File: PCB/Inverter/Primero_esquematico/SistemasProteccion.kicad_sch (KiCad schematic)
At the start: 34 parts, among them U22 TLV1704AQPWRQ1, U23 TLV1704AQPWRQ1

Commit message: Esquematico practicamente terminado
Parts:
- C77, C78, C79, C80: footprint (none) -> Capacitor_SMD:C_0603_1608Metric
- R143, R144, R145, R146, R147, R148, R149, R150, R151, R152, R153, R154, R155, R156, R157, R158, R159, R160, R161, R162, R163, R164, R165, R166, R167, R168, R169, R170: footprint (none) -> Resistor_SMD:R_0402_1005Metric
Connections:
- net +3.3V_ref renamed +3V0
- removed net ErrorFlag: R144.2, R145.2, R155.2, R156.2, R162.2, R163.2, R164.2, R165.2, U22.1 (2OUT), U22.13 (4OUT), U22.14 (3OUT), U22.2 (1OUT), U23.1 (2OUT), U23.13 (4OUT), U23.14 (3OUT), U23.2 (1OUT)
- new net Error_Current_Fase_A: R144.2, R145.2, U22.1 (2OUT), U22.2 (1OUT)
- new net Error_Current_Fase_B: R155.2, R156.2, U22.13 (4OUT), U22.14 (3OUT)
- new net Error_Current_Fase_C: R162.2, R163.2, U23.1 (2OUT), U23.2 (1OUT)
- new net Error_DC: R164.2, R165.2, U23.13 (4OUT), U23.14 (3OUT)
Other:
- note added: "CALCULAR LOS LIMITE"
- note added: "Transferencia de tension medida y lo que ve el sensor en este bloque: V_sensor=V_dc.11,52mV/V-1,411V"

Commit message: Un par de cosas q corregi del ERC pero sigue mal
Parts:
- U22, U23: footprint Snapeda:PW14_TEX-L -> PW14_TEX
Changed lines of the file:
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@@
 			)
 		)
-		(property "Footprint" "Snapeda:PW14_TEX-L"
+		(property "Footprint" "PW14_TEX"
 			(at 100.33 139.7 0)
 			(hide yes)
@@
 			)
 		)
-		(property "Footprint" "Snapeda:PW14_TEX-L"
+		(property "Footprint" "PW14_TEX"
 			(at 99.06 80.01 0)
 			(hide yes)

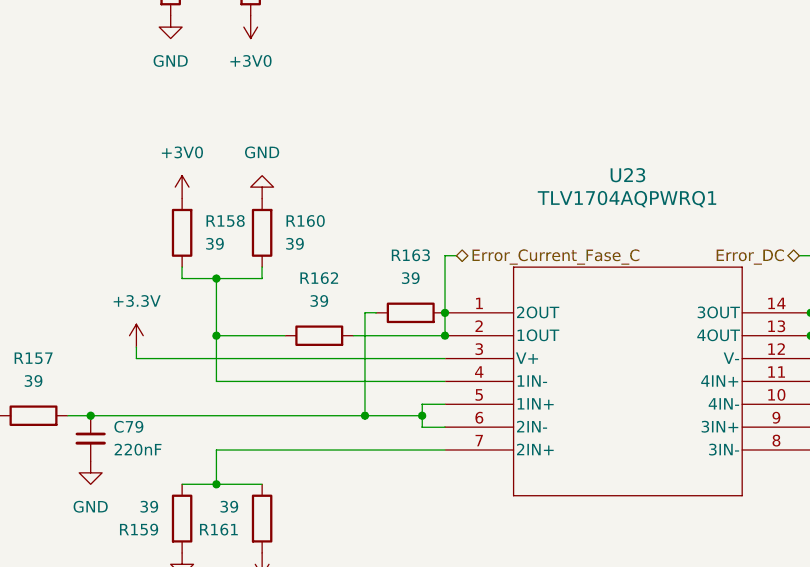
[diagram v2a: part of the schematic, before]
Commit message: Esquematico Listo
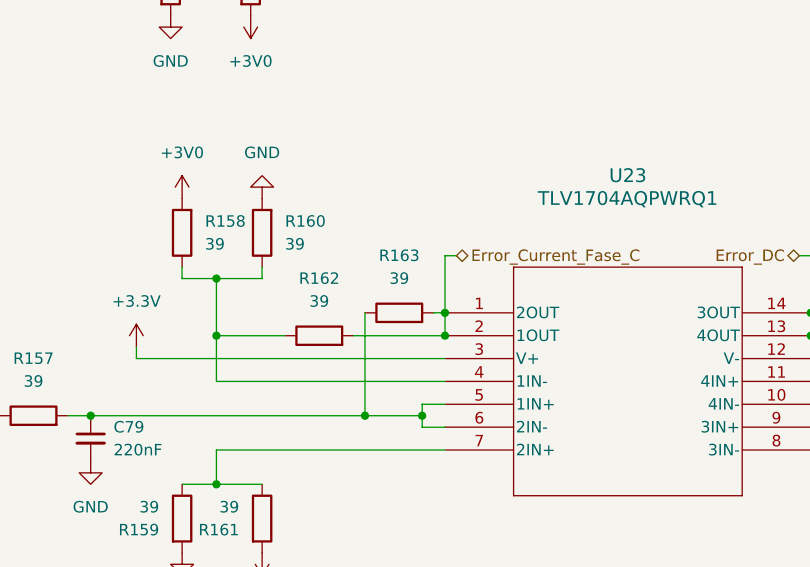
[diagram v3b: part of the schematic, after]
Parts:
- U22, U23: footprint PW14_TEX -> Snapeda:PW14_TEX-L
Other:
- moved on the sheet: R163
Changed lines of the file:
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@@
 	(wire
 		(pts
-			(xy 71.12 149.86) (xy 72.39 149.86)
-		)
-		(stroke
-			(width 0)
-			(type default)
-		)
-	)
-	(wire
-		(pts
 			(xy 148.59 86.36) (xy 144.78 86.36)
 		)
@@
 	(wire
 		(pts
+			(xy 78.74 149.86) (xy 80.01 149.86)
+		)
+		(stroke
+			(width 0)
+			(type default)
+		)
+	)
+	(wire
+		(pts
 			(xy 69.85 90.17) (xy 69.85 101.6)
 		)
@@
 	(symbol
 		(lib_id "Device:R")
-		(at 76.2 149.86 90)
+		(at 74.93 149.86 90)
 		(unit 1)
 		(body_style 1)
@@
 		(fields_autoplaced yes)
 		(property "Reference" "R163"
-			(at 76.2 143.51 90)
+			(at 74.93 143.51 90)
 			(show_name no)
 			(do_not_autoplace no)
@@
 		)
 		(property "Value" "39"
-			(at 76.2 146.05 90)
+			(at 74.93 146.05 90)
 			(show_name no)
 			(do_not_autoplace no)
@@
 		)
 		(property "Footprint" "Resistor_SMD:R_0402_1005Metric"
-			(at 76.2 151.638 90)
+			(at 74.93 151.638 90)
 			(hide yes)
 			(show_name no)
@@
 		)
 		(property "Datasheet" ""
-			(at 76.2 149.86 0)
+			(at 74.93 149.86 0)
 			(hide yes)
 			(show_name no)
@@
 		)
 		(property "Description" "Resistor"
-			(at 76.2 149.86 0)
+			(at 74.93 149.86 0)
 			(hide yes)
 			(show_name no)
@@
 			)
 		)
-		(property "Footprint" "PW14_TEX"
+		(property "Footprint" "Snapeda:PW14_TEX-L"
 			(at 100.33 139.7 0)
 			(hide yes)
@@
 			)
 		)
-		(property "Footprint" "PW14_TEX"
+		(property "Footprint" "Snapeda:PW14_TEX-L"
 			(at 99.06 80.01 0)
 			(hide yes)

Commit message: correcciones
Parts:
- renumbered C77 to C127, C79 to C128, C78 to C129, C80 to C130, R143 to R162, R157 to R163, R146 to R164, R149 to R165, R158 to R166, R159 to R167, R147 to R168, R148 to R169, R160 to R170, R161 to R171, R145 to R172, R162 to R173, R144 to R174, R163 to R175, R156 to R176, R164 to R177, R155 to R178, R165 to R179, R153 to R180, R154 to R181, R166 to R182, R167 to R183, R151 to R184, R152 to R185, R168 to R186, R169 to R187, R150 to R188, R170 to R189, U22 to U29, U23 to U30

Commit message: Algunos cambios
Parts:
- C127, C128, C129, C130: footprint Capacitor_SMD:C_0603_1608Metric -> Capacitor_SMD:C_0402_1005Metric
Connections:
- net +3.3V renamed +3.3V_analog

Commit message: Corregi cosas de la placa
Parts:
- renumbered C127 to C147, C128 to C148, C129 to C149, C130 to C150, U29 to U28, U30 to U29
